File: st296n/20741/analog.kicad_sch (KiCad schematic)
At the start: 189 parts, among them J3 POWER, J4 SPINDLE, J5 STEPPER, J6 HEADS, Q1 ?, Q10 ?, Q11 ?, Q12 ?, Q15 "1A", Q2 2SD1760, Q3 IRFD110, Q4 IRFD110, Q5 IRFD110, Q8 ?, Q9 ?, U27 74LS00, U3 74LS14, U8 11747-501

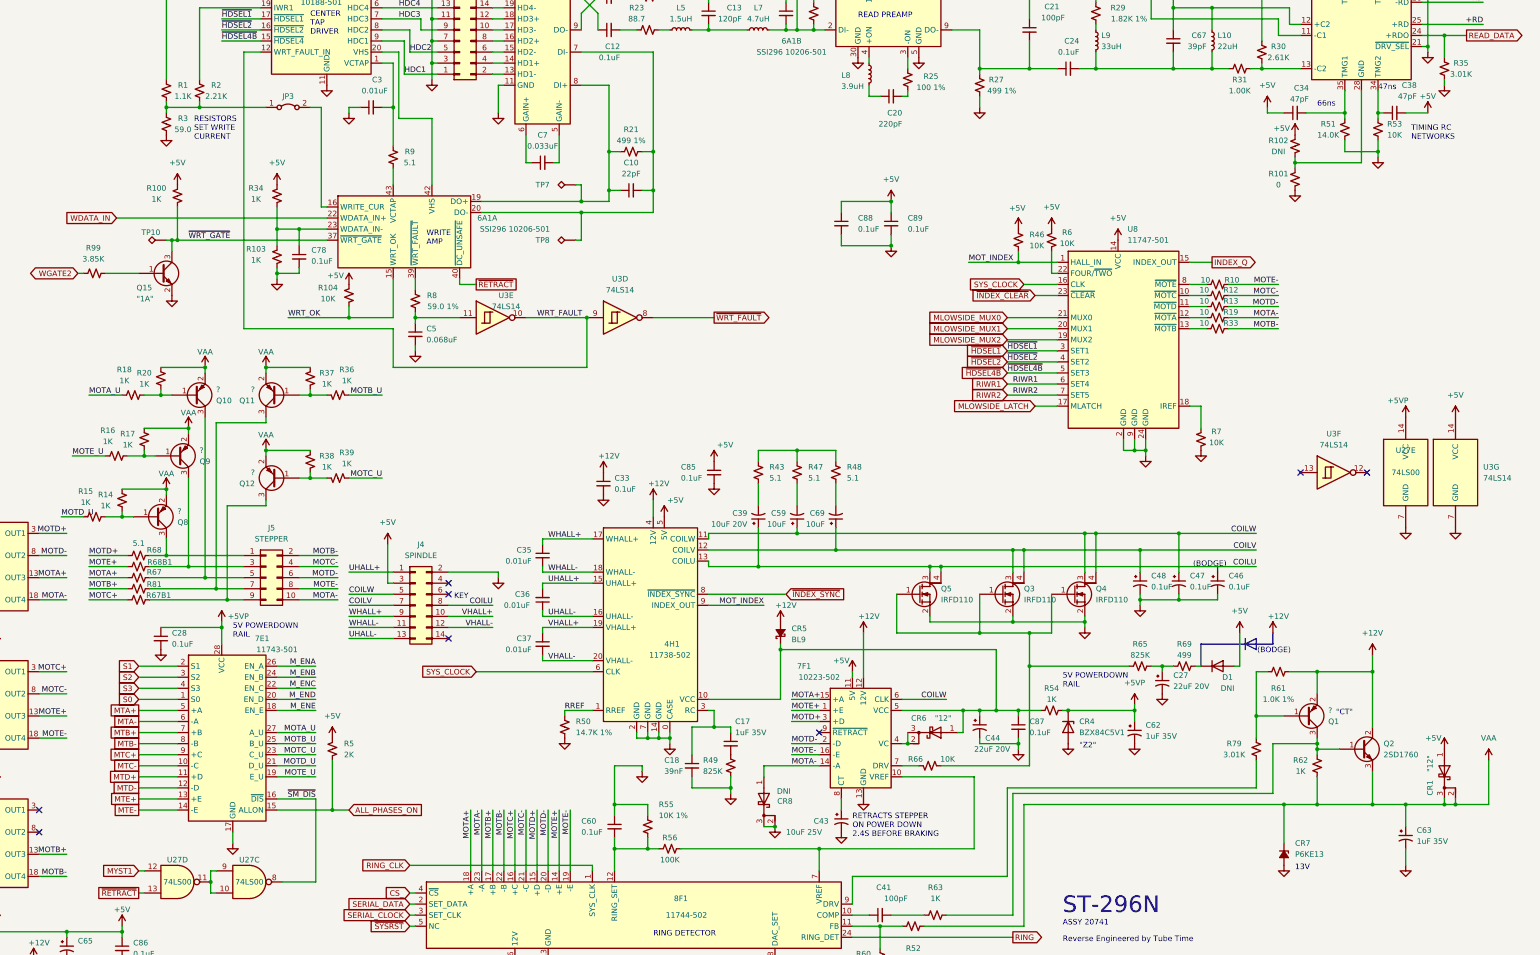
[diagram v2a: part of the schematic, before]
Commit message: Add ST-251N. Update ST-296N to show changes.
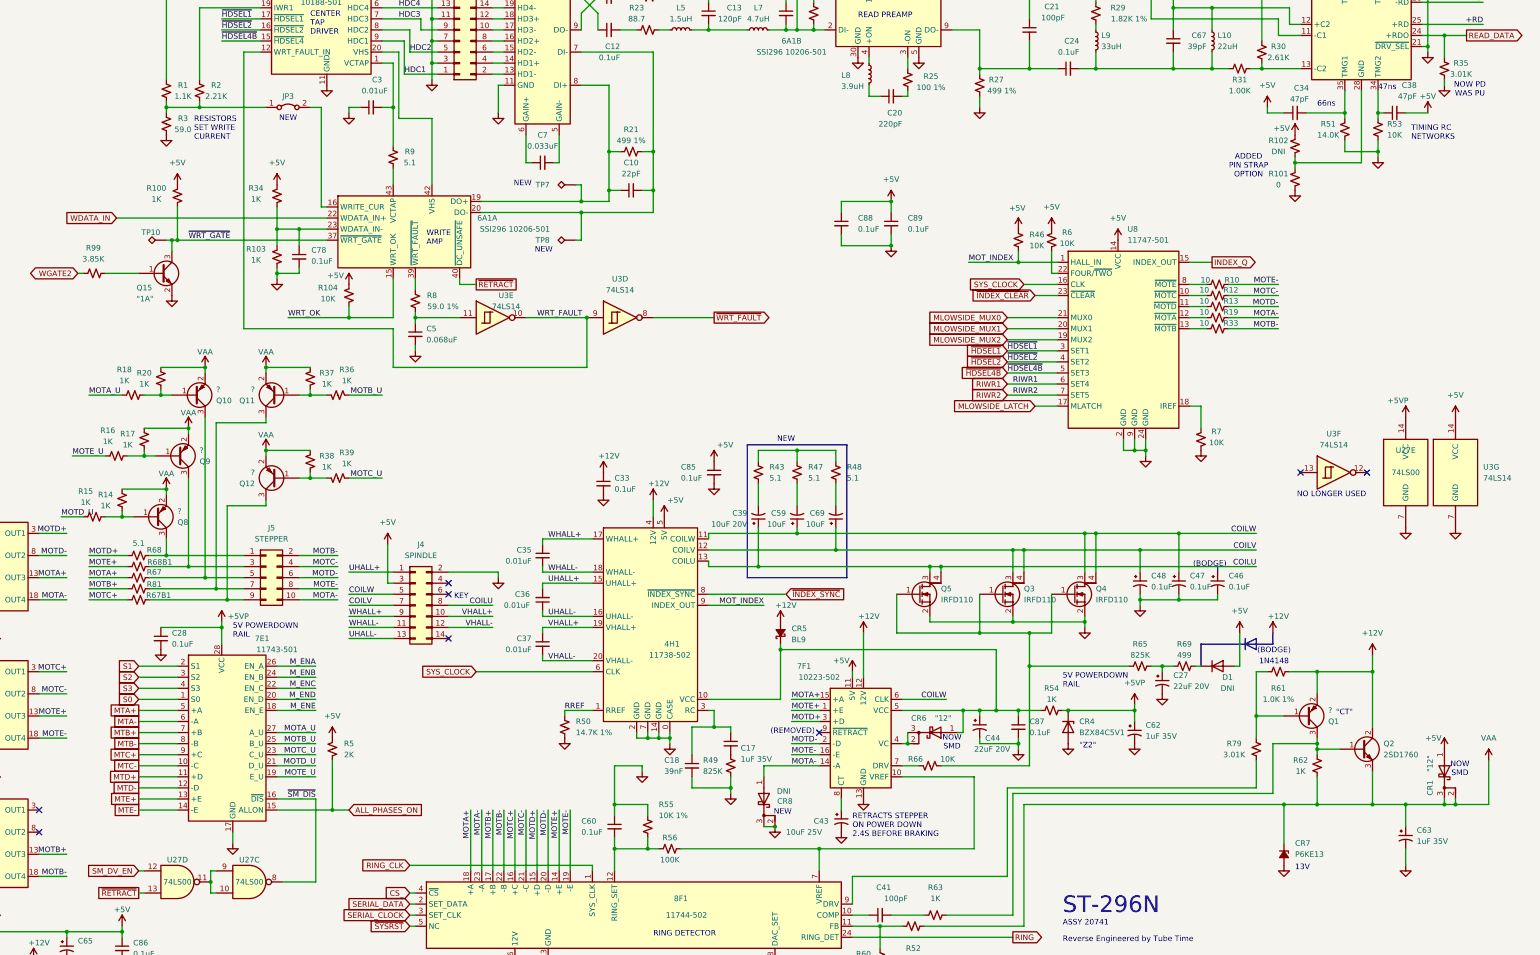
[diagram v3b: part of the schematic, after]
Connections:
- net MYST1 renamed SM_DV_EN
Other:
- note added: "(REMOVED)"
- note added: "1N4148"
- note added: "ADDED PIN STRAP OPTION"
- note added: "NEW"
- note added: "NO LONGER USED"
- note added: "NOW PD WAS PU"
- note added: "NOW SMD"
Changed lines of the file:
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@@
 		)
 	)
+	(rectangle
+		(start 229.87 152.4)
+		(end 252.73 182.88)
+		(stroke
+			(width 0)
+			(type default)
+			(color 255 0 255 1)
+		)
+		(fill
+			(type none)
+		)
+	)
+	(text "NOW PD\nWAS PU"
+		(exclude_from_sim no)
+		(at 395.732 70.866 0)
+		(effects
+			(font
+				(size 1.27 1.27)
+				(color 255 0 255 1)
+			)
+		)
+	)
 	(text "HEAD CENTER\nTAP CONNS"
 		(exclude_from_sim no)
@@
 		)
 	)
+	(text "NEW"
+		(exclude_from_sim no)
+		(at 238.76 151.13 0)
+		(effects
+			(font
+				(size 1.27 1.27)
+				(color 255 0 255 1)
+			)
+		)
+	)
 	(text "TBDKHz to TBDMHz BPF"
 		(exclude_from_sim no)
@@
 		)
 	)
+	(text "NEW"
+		(exclude_from_sim no)
+		(at 183.134 107.696 0)
+		(effects
+			(font
+				(size 1.27 1.27)
+				(color 255 0 255 1)
+			)
+		)
+	)
 	(text "47ns"
 		(exclude_from_sim no)
@@
 		)
 	)
+	(text "(REMOVED)"
+		(exclude_from_sim no)
+		(at 240.284 218.186 0)
+		(effects
+			(font
+				(size 1.27 1.27)
+				(color 255 0 255 1)
+			)
+		)
+	)
+	(text "1N4148"
+		(exclude_from_sim no)
+		(at 350.774 202.184 0)
+		(effects
+			(font
+				(size 1.27 1.27)
+			)
+		)
+	)
 	(text "Reverse Engineered by Tube Time"
 		(exclude_from_sim no)
@@
 		)
 	)
+	(text "ADDED\nPIN STRAP\nOPTION"
+		(exclude_from_sim no)
+		(at 344.932 88.392 0)
+		(effects
+			(font
+				(size 1.27 1.27)
+				(color 255 0 255 1)
+			)
+		)
+	)
+	(text "NO LONGER USED"
+		(exclude_from_sim no)
+		(at 363.982 163.83 0)
+		(effects
+			(font
+				(size 1.27 1.27)
+				(color 255 0 255 1)
+			)
+		)
+	)
 	(text "5V POWERDOWN\nRAIL"
 		(exclude_from_sim no)
@@
 		)
 	)
+	(text "NOW\nSMD"
+		(exclude_from_sim no)
+		(at 393.446 226.822 0)
+		(effects
+			(font
+				(size 1.27 1.27)
+				(color 255 0 255 1)
+			)
+		)
+	)
 	(text "5V POWERDOWN\nRAIL"
 		(exclude_from_sim no)
@@
 		)
 	)
+	(text "NEW"
+		(exclude_from_sim no)
+		(at 237.998 236.728 0)
+		(effects
+			(font
+				(size 1.27 1.27)
+				(color 255 0 255 1)
+			)
+		)
+	)
 	(text "66ns"
 		(exclude_from_sim no)
@@
 		)
 	)
+	(text "NEW"
+		(exclude_from_sim no)
+		(at 178.308 92.456 0)
+		(effects
+			(font
+				(size 1.27 1.27)
+				(color 255 0 255 1)
+			)
+		)
+	)
 	(text "CENTER\nTAP\nDRIVER"
 		(exclude_from_sim no)
@@
 		)
 	)
+	(text "NEW"
+		(exclude_from_sim no)
+		(at 124.46 77.47 0)
+		(effects
+			(font
+				(size 1.27 1.27)
+				(color 255 0 255 1)
+			)
+		)
+	)
 	(text "This work is licensed under a Creative Commons\nAttribution-ShareAlike 4.0 International License.\nSee https://creativecommons.org/licenses/by-sa/4.0/.\n"
 		(exclude_from_sim no)
@@
 		)
 	)
+	(text "NOW\nSMD"
+		(exclude_from_sim no)
+		(at 276.86 220.726 0)
+		(effects
+			(font
+				(size 1.27 1.27)
+				(color 255 0 255 1)
+			)
+		)
+	)
 	(label "MOTD-"
 		(at 73.66 177.8 180)
@@
 		)
 	)
-	(global_label "MYST1"
+	(global_label "SM_DV_EN"
 		(shape input)
 		(at 90.17 250.19 180)
@@
 		)
 		(property "Intersheetrefs" "${INTERSHEET_REFS}"
-			(at 81.2582 250.19 0)
+			(at 77.7506 250.19 0)
 			(effects
 				(font
@@
 				(font
 					(size 1.27 1.27)
-					(color 255 0 255 1)
 				)
 			)
@@
 				(font
 					(size 1.27 1.27)
+					(color 255 0 255 1)
 				)
 			)
@@
 				(font
 					(size 1.27 1.27)
+					(color 255 0 255 1)
 				)
 				(justify left)
@@
 				(font
 					(size 1.27 1.27)
+					(color 255 0 255 1)
 				)
 				(justify right)
@@
 				(font
 					(size 1.27 1.27)
+					(color 255 0 255 1)
 				)
 			)
@@
 				(font
 					(size 1.27 1.27)
+					(color 255 0 255 1)
 				)
 			)
@@
 				(font
 					(size 1.27 1.27)
+					(color 255 0 255 1)
 				)
 			)
@@
 				(font
 					(size 1.27 1.27)
+					(color 255 0 255 1)
 				)
 			)
@@
 				(font
 					(size 1.27 1.27)
+					(color 255 0 255 1)
 				)
 			)
@@
 				(font
 					(size 1.27 1.27)
+					(color 255 0 255 1)
 				)
 			)
@@
 		(dnp no)
 		(property "Reference" "C17"
-			(at 227.076 215.9 0)
+			(at 228.346 221.996 0)
 			(effects
 				(font
@@
 		)
 		(property "Value" "1uF 35V"
-			(at 227.076 218.44 0)
+			(at 228.346 224.536 0)
 			(effects
 				(font
 					(size 1.27 1.27)
-					(color 255 0 255 1)
 				)
 				(justify left)
@@
 				(font
 					(size 1.27 1.27)
-					(color 255 0 255 1)
 				)
 			)
@@
 				(font
 					(size 1.27 1.27)
+					(color 255 0 255 1)
 				)
 			)
@@
 				(font
 					(size 1.27 1.27)
+					(color 255 0 255 1)
 				)
 			)
@@
 				(font
 					(size 1.27 1.27)
+					(color 255 0 255 1)
 				)
 			)
@@
 				(font
 					(size 1.27 1.27)
+					(color 255 0 255 1)
 				)
 			)
@@
 				(font
 					(size 1.27 1.27)
+					(color 255 0 255 1)
 				)
 			)
@@
 				(font
 					(size 1.27 1.27)
+					(color 255 0 255 1)
 				)
 			)
@@
 				(font
 					(size 1.27 1.27)
-					(color 255 0 255 1)
 				)
 			)
@@
 				(font
 					(size 1.27 1.27)
-					(color 255 0 255 1)
 				)
 				(justify right)
@@
 				(font
 					(size 1.27 1.27)
+					(color 255 0 255 1)
 				)
 				(justify right)
@@
 				(font
 					(size 1.27 1.27)
+					(color 255 0 255 1)
 				)
 			)
@@
 				(font
 					(size 1.27 1.27)
+					(color 255 0 255 1)
 				)
 			)
